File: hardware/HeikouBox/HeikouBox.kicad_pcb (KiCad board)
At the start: 2 copper layers, 100 x 100 mm, 196 parts, among them J101 5V, J201 Conn_02x05_Odd_Even, J202 Conn_02x08_Odd_Even, J301 DB15_Female_HighDensity_Mount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, J302 AudioJack3_SwitchTR, J501 Micro_SD_Card_TFP09-2-12B, J503 PS/2, Q301 MMBT3904, Q302 MMBT3904, Q303 MMBT3904, Q304 MMBT3904, Q305 MMBT3904, Q306 MMBT3904, Q307 MMBT3904, Q502 BSS138, Q503 BSS138, SW501 Left, SW502 Right, SW503 Up, SW504 Down, U101 LD1117S33TR, U102 LD1117S25TR, U103 LD1117S12TR, U201 HeikouBox-Core, U202 74HCU04, U401 K4S281632-UC60, U501 STM32-BluePill-Socket, Y201 14.31818MHz, Y202 28.37516MHz

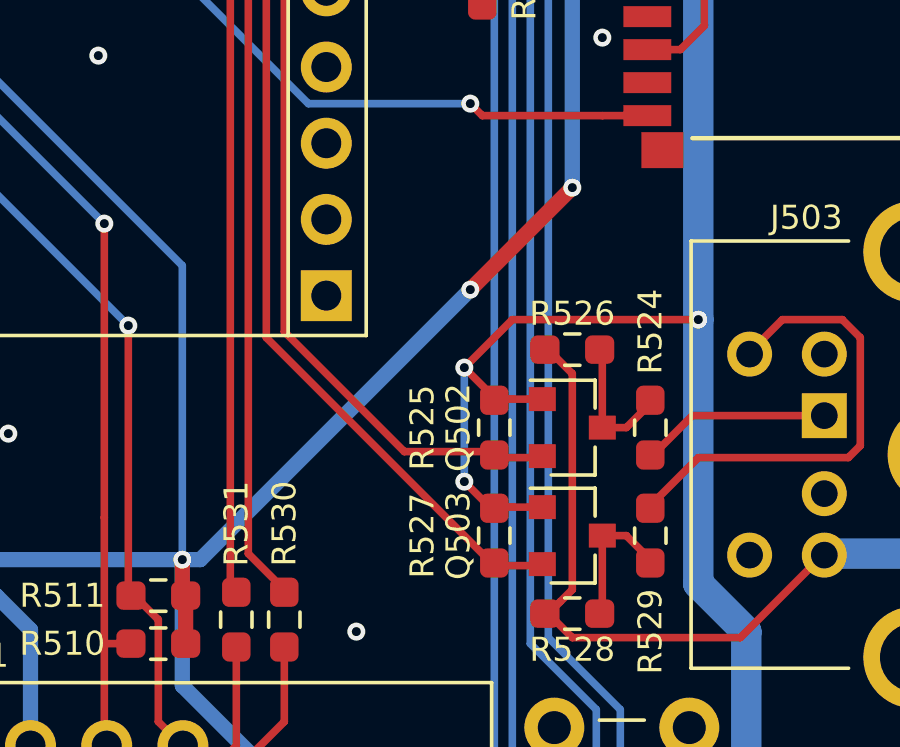
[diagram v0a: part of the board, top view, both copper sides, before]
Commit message: Update regulator capacitor values
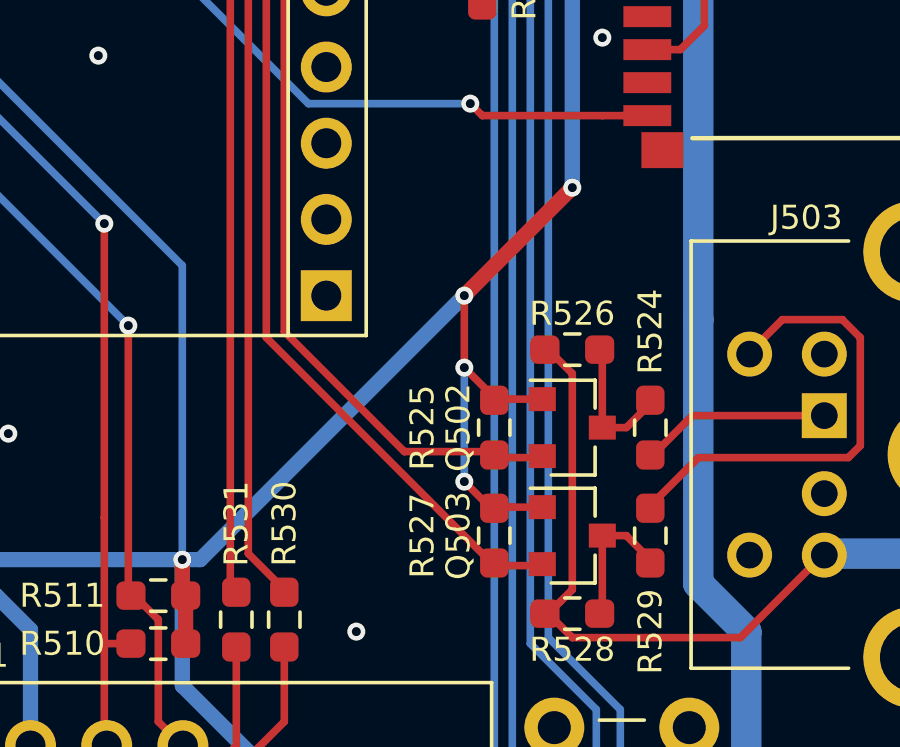
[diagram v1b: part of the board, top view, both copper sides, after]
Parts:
- C101, C104, C105, C106: value 10u -> 22u
- R101: value 1K -> 10K
- R524, R529: value 100R -> 75R
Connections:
- Q502 pad 1: /part1-power/3V3 -> /part5-hub/3V3_HUB
- Q503 pad 1: /part1-power/3V3 -> /part5-hub/3V3_HUB
- R525 pad 2: /part1-power/3V3 -> /part5-hub/3V3_HUB
- R527 pad 2: /part1-power/3V3 -> /part5-hub/3V3_HUB
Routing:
- net /part1-power/3V3: track 556.6 -> 538.2 mm, vias 29 -> 26
- net /part5-hub/3V3_HUB: track 198.6 -> 210.9 mm, vias 9 -> 11

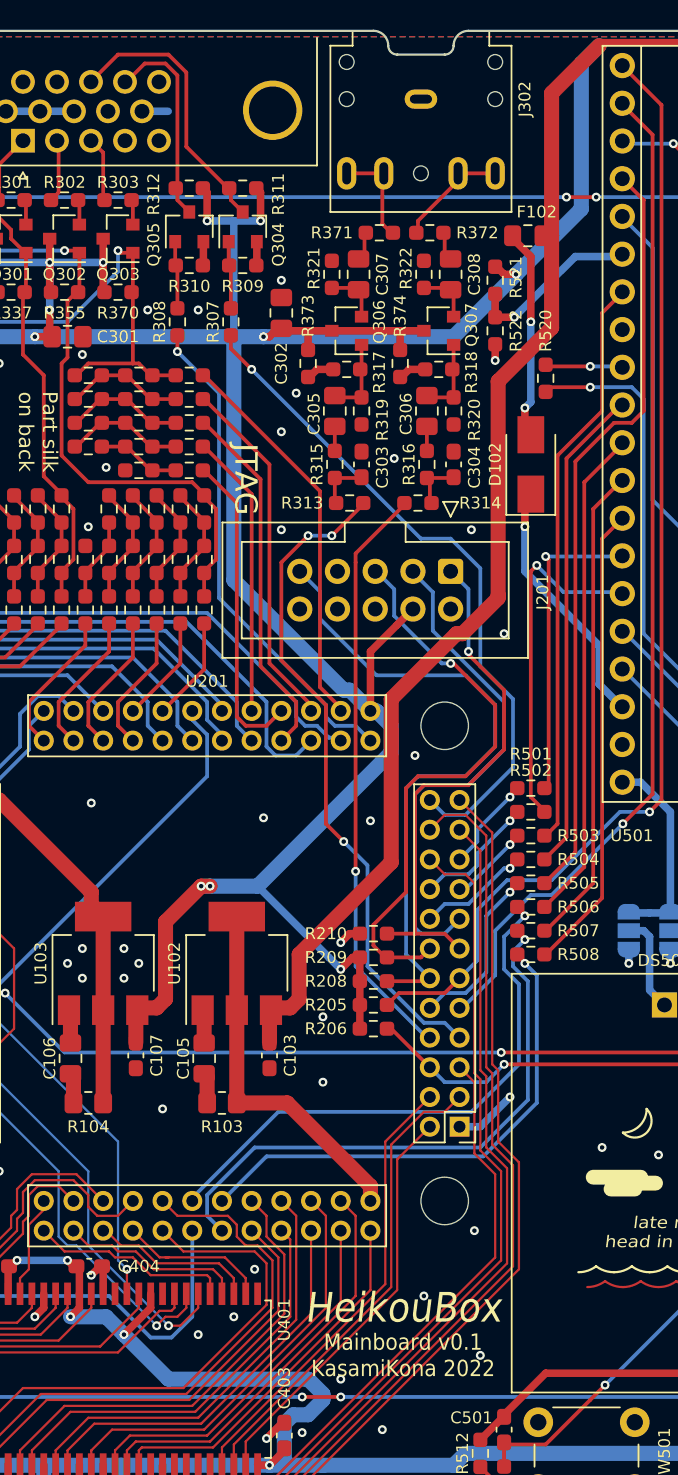
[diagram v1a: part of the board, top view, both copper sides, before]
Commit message: Add VGA sync invert jumpers
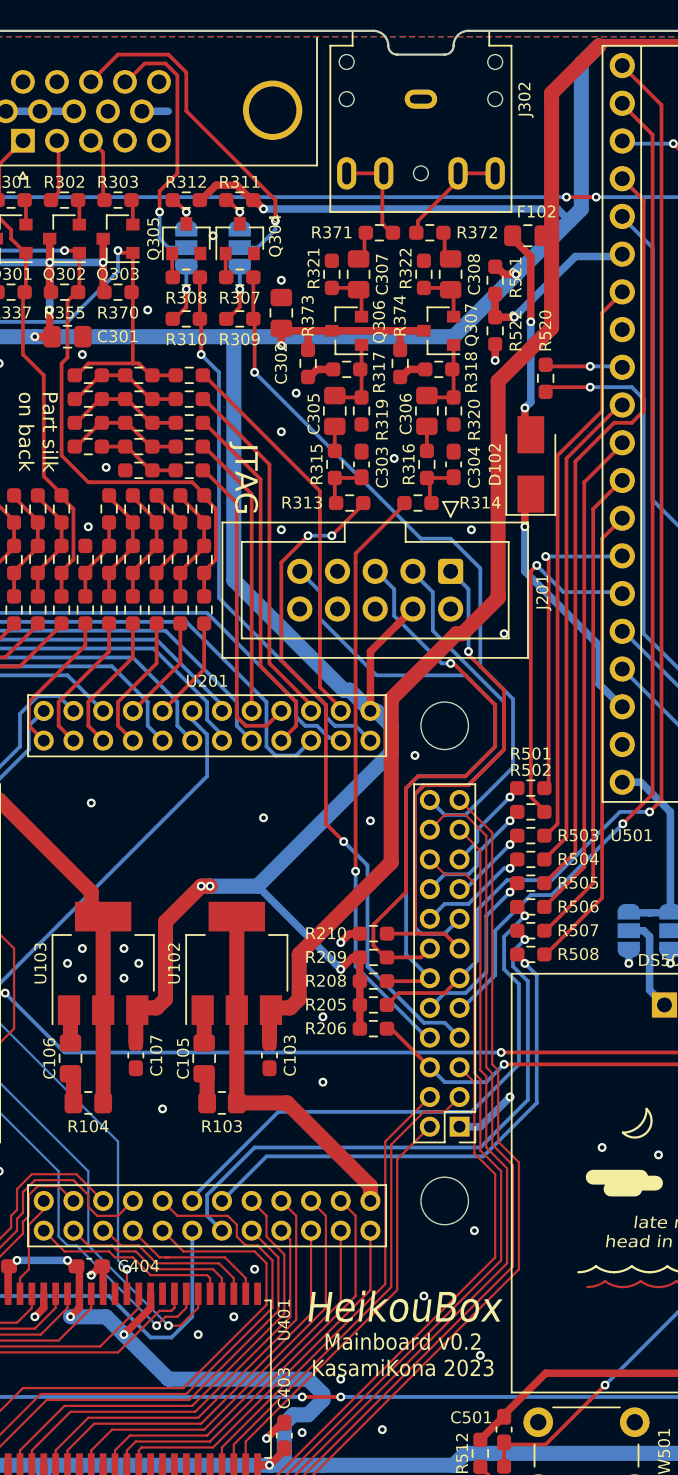
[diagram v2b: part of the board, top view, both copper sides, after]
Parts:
- added JP301: HS, Jumper:SolderJumper-3_P1.3mm_Open_RoundedPad1.0x1.5mm, B.Cu at (48.4, 35.0)
- added JP302: HS, Jumper:SolderJumper-3_P1.3mm_Open_RoundedPad1.0x1.5mm, B.Cu at (44.8, 35.0)
- R311, R312: value 2K2 -> 1K
- moved R309 3.61 mm to (48.4, 39.8), turned to 180 degrees
- moved R310 3.61 mm to (44.8, 39.8), turned to 180 degrees
- moved R307 3.06 mm to (48.4, 37.0), turned to 180 degrees
- moved R308 3.06 mm to (44.8, 37.0), turned to 180 degrees
- moved R311 0.82 mm to (48.4, 31.8)
- moved R312 0.82 mm to (44.8, 31.8)
- moved Q304 0.82 mm to (48.4, 34.4)
- moved Q305 0.82 mm to (44.8, 34.4)
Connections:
- Q304 pad 3: Net-(J301-Pad13) -> Net-(JP301-Pad1)
- Q305 pad 3: Net-(J301-Pad14) -> Net-(JP302-Pad1)
- R309 pad 1: Net-(Q304-Pad1) -> /part3-av/NHSYNC
- R309 pad 2: /part1-power/GND -> Net-(JP301-Pad3)
- R310 pad 1: Net-(Q305-Pad1) -> /part3-av/NVSYNC
- R310 pad 2: /part1-power/GND -> Net-(JP302-Pad3)
- R311 pad 2: Net-(J301-Pad13) -> Net-(JP301-Pad1)
- R312 pad 2: Net-(J301-Pad14) -> Net-(JP302-Pad1)
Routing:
- net /part1-power/3V3: track 538.2 -> 548.9 mm, vias 26 -> 25
- net Net-(J301-Pad13): track 18.7 -> 23.7 mm, vias 0 -> 1
- net Net-(JP301-Pad3): track 0.00 -> 3.94 mm, vias 0 -> 1
- net Net-(JP302-Pad3): track 0.00 -> 3.94 mm, vias 0 -> 1
- net Net-(J301-Pad14): track 14.0 -> 17.9 mm, vias 0 -> 1
- net /part3-av/NVSYNC: track 33.5 -> 36.8 mm
- net /part3-av/NHSYNC: track 45.5 -> 48.8 mm
- net Net-(JP302-Pad1): track 0.00 -> 3.27 mm, vias 0 -> 1
- net /part1-power/GND: track 75.1 -> 71.8 mm
- net Net-(JP301-Pad1): track 0.00 -> 3.14 mm, vias 0 -> 1
- net Net-(Q305-Pad1): track 4.55 -> 1.62 mm
- net Net-(Q304-Pad1): track 4.55 -> 1.62 mm
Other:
- board text added: "Mainboard v0.2 KasamiKona 2023"
- board text added: "SYNC INV"
- board text removed: "Mainboard v0.1 KasamiKona 2022"

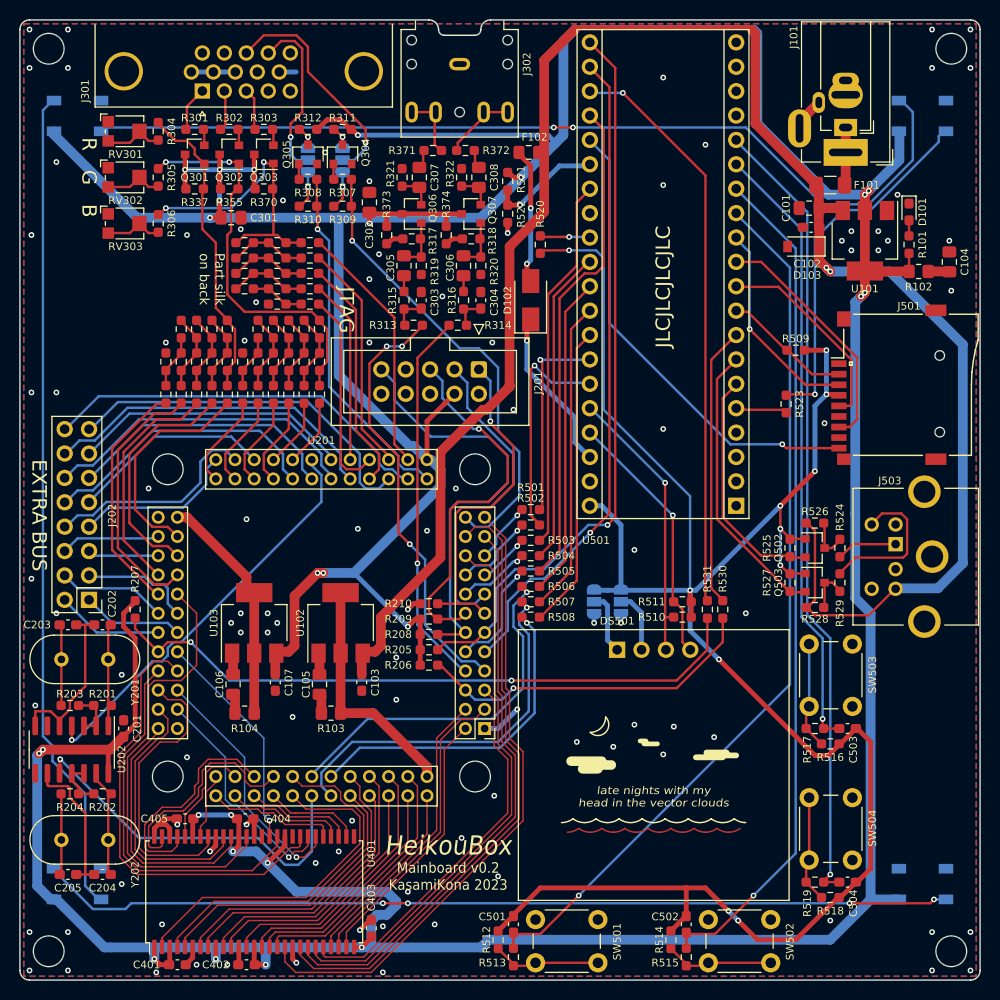
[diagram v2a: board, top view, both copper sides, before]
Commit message: Remove these dumb mounting holes for core
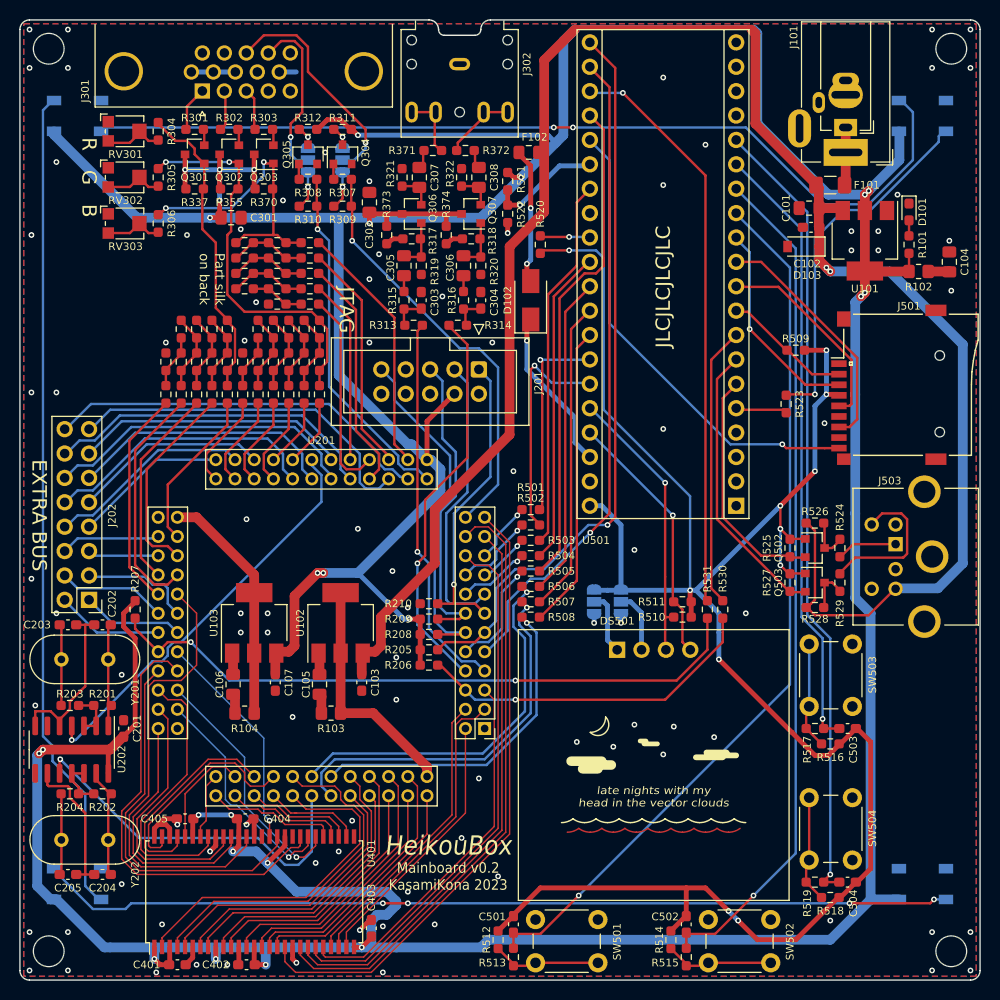
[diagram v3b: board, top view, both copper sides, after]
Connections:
- J101 pad 3: Net-(J101-Pad3) -> /part1-power/GND
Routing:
- net /part2-core/jtag_TDI: track 44.4 -> 36.5 mm
- net /part3-av/RED4: track 23.1 -> 16.9 mm
- net /part2-core/jtag_TMS: track 38.7 -> 32.6 mm, vias 1 -> 0
- net /part1-power/GND: track 71.8 -> 66.1 mm, vias 99 -> 91
- net /part3-av/LSIGMA: track 45.0 -> 39.9 mm, vias 3 -> 1
- net /part3-av/NHSYNC: track 48.8 -> 44.1 mm
- net /part2-core/jtag_TDO: track 34.4 -> 30.0 mm
- net /part2-core/jtag_TCK: track 35.4 -> 31.8 mm
- net Net-(J101-Pad3): track 3.53 -> 0.00 mm
- net /part3-av/RED3: track 24.4 -> 21.0 mm
- net /part3-av/RED2: track 24.0 -> 21.0 mm
- net /part3-av/RED1: track 27.1 -> 24.5 mm
- net /part3-av/RED0: track 24.8 -> 22.8 mm
- net /part2-core/mdb5: track 37.7 -> 39.4 mm
- net /part3-av/RSIGMA: track 39.5 -> 41.1 mm
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
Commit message: Cleanup routing
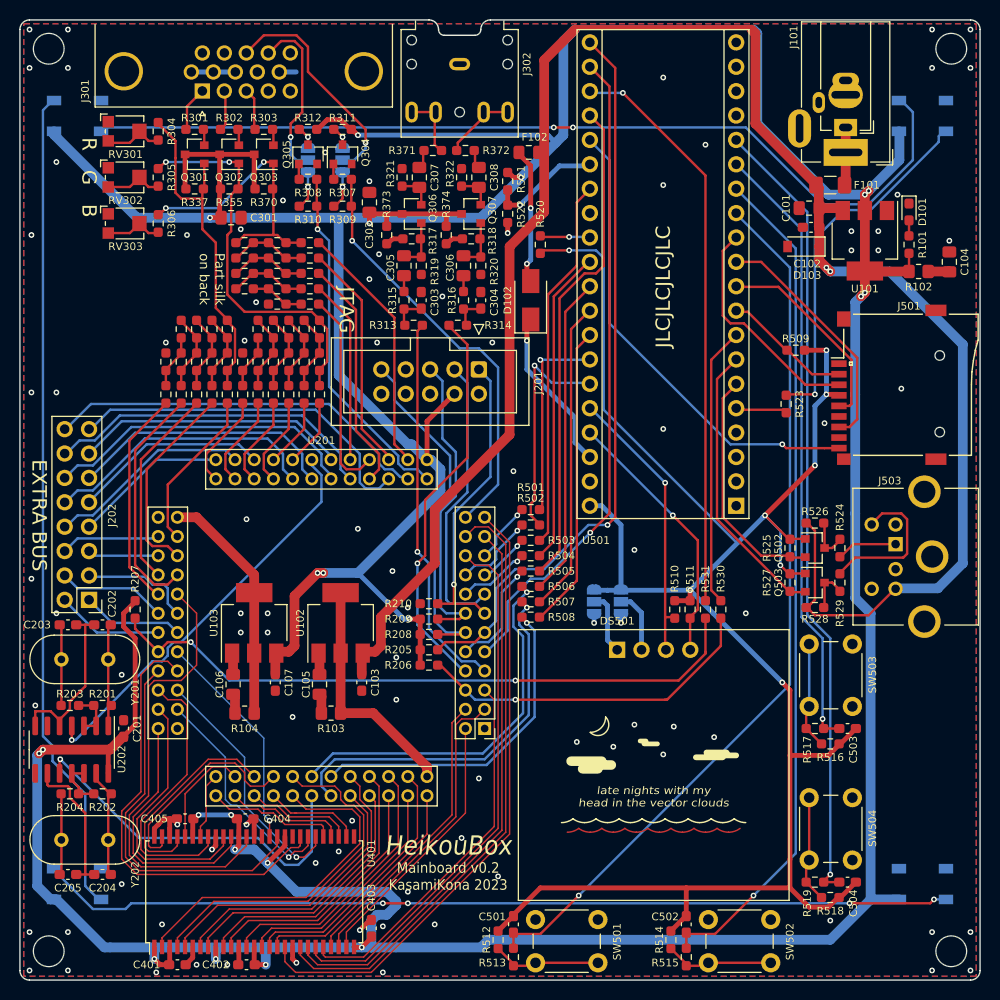
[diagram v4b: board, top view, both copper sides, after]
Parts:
- moved R510 1.13 mm to (83.0, 81.8), turned to 90 degrees
- moved R511 1.13 mm to (84.6, 81.8), turned to 90 degrees
- moved R530 0.20 mm to (87.8, 81.8)
- moved R531 0.20 mm to (86.2, 81.8)
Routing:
- net /part5-hub/3V3_HUB: track 210.6 -> 204.4 mm, vias 11 -> 8
- net Net-(Q301-Pad1): track 31.9 -> 36.1 mm
- net /part1-power/3V3: track 548.1 -> 545.7 mm, vias 25 -> 21
- net /part5-hub/SD_MOSI: track 21.8 -> 23.8 mm, vias 1 -> 0
- net Net-(Q303-Pad1): track 30.1 -> 29.3 mm
- net /part1-power/GND: track 66.1 -> 65.4 mm, vias 91 -> 93
- net /part5-hub/OLED_SDA: track 27.0 -> 27.6 mm
- net (no net): vias 2 -> 0

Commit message: Routing cleanup, rearrange neopixels again... Do I really need these?
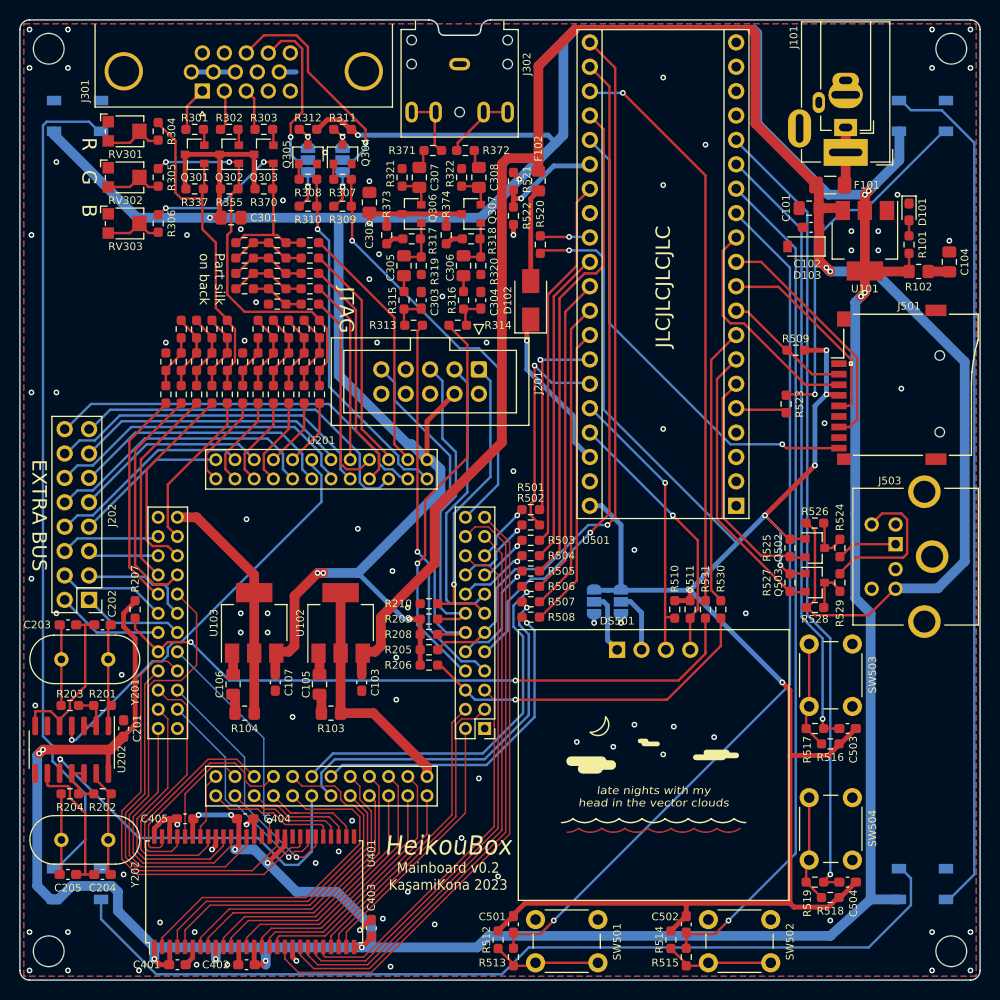
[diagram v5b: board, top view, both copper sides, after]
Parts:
- moved D502 118.9 mm to (108.8, 110.4)
- moved D504 118.9 mm to (20.8, 30.4)
- moved F102 3.14 mm to (68.8, 37.2), turned to 270 degrees
- moved R522 0.63 mm to (66.2, 40.8)
- moved R521 0.60 mm to (66.2, 37.2)
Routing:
- net Net-(D502-Pad2): track 86.4 -> 96.6 mm
- net Net-(D503-Pad2): track 95.1 -> 87.3 mm, vias 4 -> 0
- net Net-(D501-Pad2): track 96.9 -> 89.9 mm, vias 2 -> 0
- net Net-(D102-Pad2): track 14.2 -> 9.73 mm, vias 2 -> 0
- net /part1-power/3V3: track 545.7 -> 541.7 mm
- net /part1-power/5V: track 196.1 -> 198.0 mm
- net /part5-hub/3V3_HUB: track 204.4 -> 203.1 mm
- net /part5-hub/PWR_DET: track 11.9 -> 11.2 mm
- net /part1-power/GND: track 65.4 -> 65.2 mm, vias 93 -> 94
